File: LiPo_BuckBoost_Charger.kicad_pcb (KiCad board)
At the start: 2 copper layers, 51 parts, among them J1 Type-C_6P, J2 JST PH Connector, J3 Conn_01x01, J4 Conn_01x01, J5 JST PH Connector, J6 Conn_01x01, J7 Conn_01x01, U1 TP4056, U2 DW01A, U3 FS8205A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

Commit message: added schematic and 3d img
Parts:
- added H1: MountingHole, MountingHole:MountingHole_3.2mm_M3_DIN965_Pad, F.Cu at (120.7, 28.3)
- added H2: MountingHole, MountingHole:MountingHole_3.2mm_M3_DIN965_Pad, F.Cu at (74.2, 50.1)
- moved JP1 2.03 mm to (94.8, 52.2)
- moved JP2 2.03 mm to (91.8, 52.2)
- moved JP3 2.03 mm to (88.8, 52.2)
- moved JP4 2.03 mm to (85.8, 52.2)
- moved JP5 2.03 mm to (82.8, 52.2)
- moved JP6 2.03 mm to (79.8, 52.2)
- moved R10 2.03 mm to (82.8, 48.3)
- moved R11 2.03 mm to (79.8, 48.3)
- moved R6 2.03 mm to (94.8, 48.4)
- moved R7 2.03 mm to (91.8, 48.4)
- moved R8 2.03 mm to (88.8, 48.4)
- moved R9 2.03 mm to (85.8, 48.3)
- moved L1 1.86 mm to (101.4, 47.4)
- moved JP7 1.79 mm to (116.2, 31.8)
- moved JP8 1.56 mm to (113.0, 31.8)
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
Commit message: some traces and gnd vias
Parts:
- moved R4 3.25 mm to (79.3, 27.7)
- moved R3 3.03 mm to (82.3, 27.7)
- moved R5 1.65 mm to (89.9, 40.6)
- moved C1 0.38 mm to (88.6, 35.5)
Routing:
- net Net-(JP1-A): track 0.00 -> 42.8 mm, vias 0 -> 2
- net Net-(D1-A): track 0.00 -> 33.2 mm, vias 0 -> 2
- net VBUS: track 0.00 -> 20.7 mm
- net GND: track 0.00 -> 13.3 mm, vias 0 -> 95
- net Net-(U1-STDBY): track 0.00 -> 13.3 mm
- net Net-(D1-K): track 0.00 -> 12.7 mm
- net Net-(U1-CHRG): track 0.00 -> 7.93 mm
- net Net-(J1-CC1): track 0.00 -> 6.54 mm
- net Net-(D2-K): track 0.00 -> 5.15 mm
- net Net-(J1-CC2): track 0.00 -> 4.88 mm
- net Net-(JP5-B): track 0.00 -> 2.20 mm
- net Net-(JP6-B): track 0.00 -> 2.19 mm
- net Net-(JP4-B): track 0.00 -> 2.19 mm
- net Net-(JP1-B): track 0.00 -> 2.18 mm
- net Net-(JP3-B): track 0.00 -> 2.18 mm
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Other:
- copper layers 2 -> 4

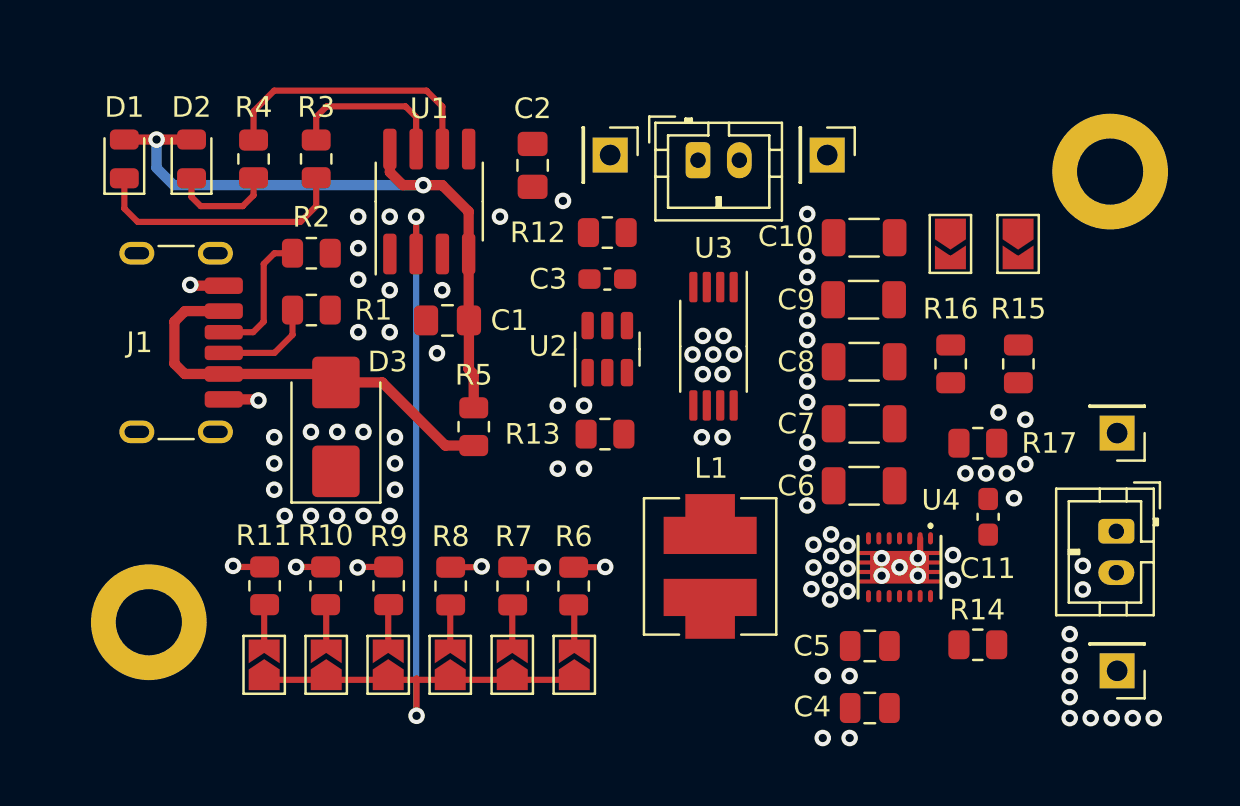
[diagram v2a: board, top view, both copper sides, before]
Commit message: Pcb traces and layout done
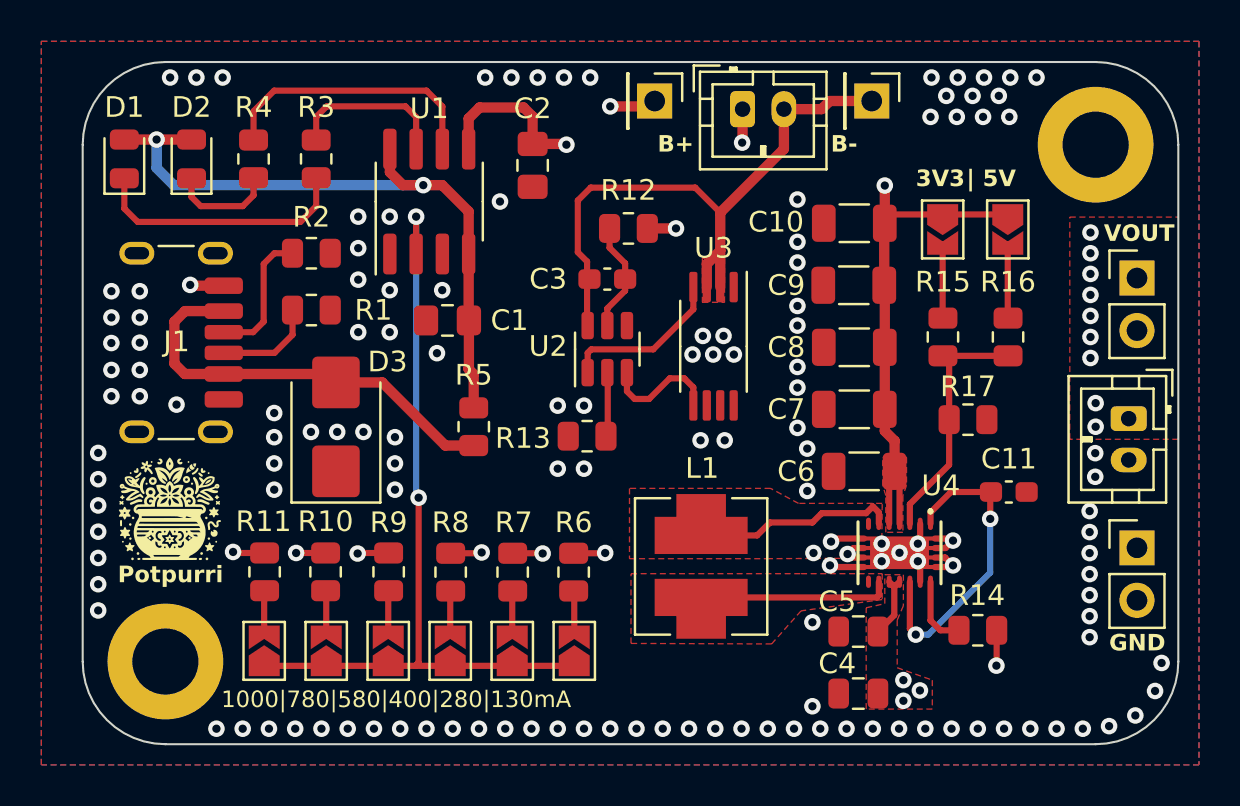
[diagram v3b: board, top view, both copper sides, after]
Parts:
- added G***: LOGO, LOGO, F.Cu at (75.2, 44.7)
- added G***: LOGO, LOGO, B.Cu at (101.7, 50.4)
- J6, J7: value Conn_01x01 -> JST PH Connector; footprint Connector_PinHeader_2.54mm:PinHeader_1x01_P2.54mm_Vertical -> Connector_PinHeader_2.54mm:PinHeader_1x02_P2.54mm_Vertical
- moved J6 7.56 mm to (122.0, 33.5), turned to 0 degrees
- moved J7 6.03 mm to (122.0, 46.5), turned to 0 degrees
- moved J5 5.48 mm to (121.6, 40.2)
- moved R15 3.88 mm to (112.6, 36.3)
- moved JP7 3.72 mm to (112.6, 31.1)
- moved J3 3.39 mm to (98.7, 24.9)
- moved J4 3.39 mm to (109.2, 24.9)
- moved J2 3.28 mm to (102.9, 25.3)
- moved R16 3.07 mm to (115.8, 36.3)
- moved JP8 2.86 mm to (115.8, 31.1)
- moved H2 2.06 mm to (75.0, 52.0)
- moved C11 1.56 mm to (115.8, 43.8), turned to 0 degrees
- moved H1 1.48 mm to (120.0, 27.0)
- moved R17 1.23 mm to (113.8, 40.3)
- moved R12 1.04 mm to (97.4, 31.1), turned to 0 degrees
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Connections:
- U4 pad 13: Net-(U4-EN) -> GND
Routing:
- net -BATT: track 0.00 -> 30.3 mm
- net +5V: track 0.00 -> 27.2 mm, vias 0 -> 11
- net +BATT: track 0.00 -> 16.5 mm, vias 0 -> 7
- net Net-(U4-EN): track 0.00 -> 15.3 mm, vias 0 -> 2
- net GND: track 13.3 -> 25.8 mm, vias 95 -> 146
- net Net-(U4-FB): track 0.00 -> 12.2 mm
- net Net-(L1-Pad2): track 0.00 -> 9.85 mm
- net Net-(L1-Pad1): track 0.00 -> 9.30 mm
- net Net-(U2-OD): track 0.00 -> 8.01 mm
- net Net-(U2-OC): track 0.00 -> 5.74 mm
- net Net-(U2-VCC): track 0.00 -> 5.44 mm
- net Net-(JP1-A): track 42.8 -> 38.7 mm
- net Net-(JP8-B): track 0.00 -> 3.57 mm
- net Net-(JP7-B): track 0.00 -> 3.57 mm
- net Net-(U4-PG): track 0.00 -> 3.45 mm
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- added copper zone on F.Cu, net +5V
- added copper zone on In2.Cu, net +5V
- added copper zone on F.Cu, net +BATT
- added copper zone on In2.Cu, net +BATT
- added copper zone on F.Cu, net -BATT
- added copper zone on B.Cu, net GND
- added copper zone on F.Cu, net GND
- added copper zone on In1.Cu, net GND
- added copper zone on F.Cu, net Net-(L1-Pad1)
- added copper zone on F.Cu, net Net-(L1-Pad2)
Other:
- board outline added: 53 x 33 mm
- board text added: "1000|780|580|400|280|130mA"
- board text added: "3V3"
- board text added: "B+"
- board text added: "B-"
- board text added: "GND"
- board text added: "Potpurri"
- board text added: "Potpurri TP4056 LiPo Charger with TPS63020 Buck-Boost Converter Version 1.0"
- board text added: "VOUT"
- board text added: "| 5V"

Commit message: added fillet tracks and tear drops to pcb
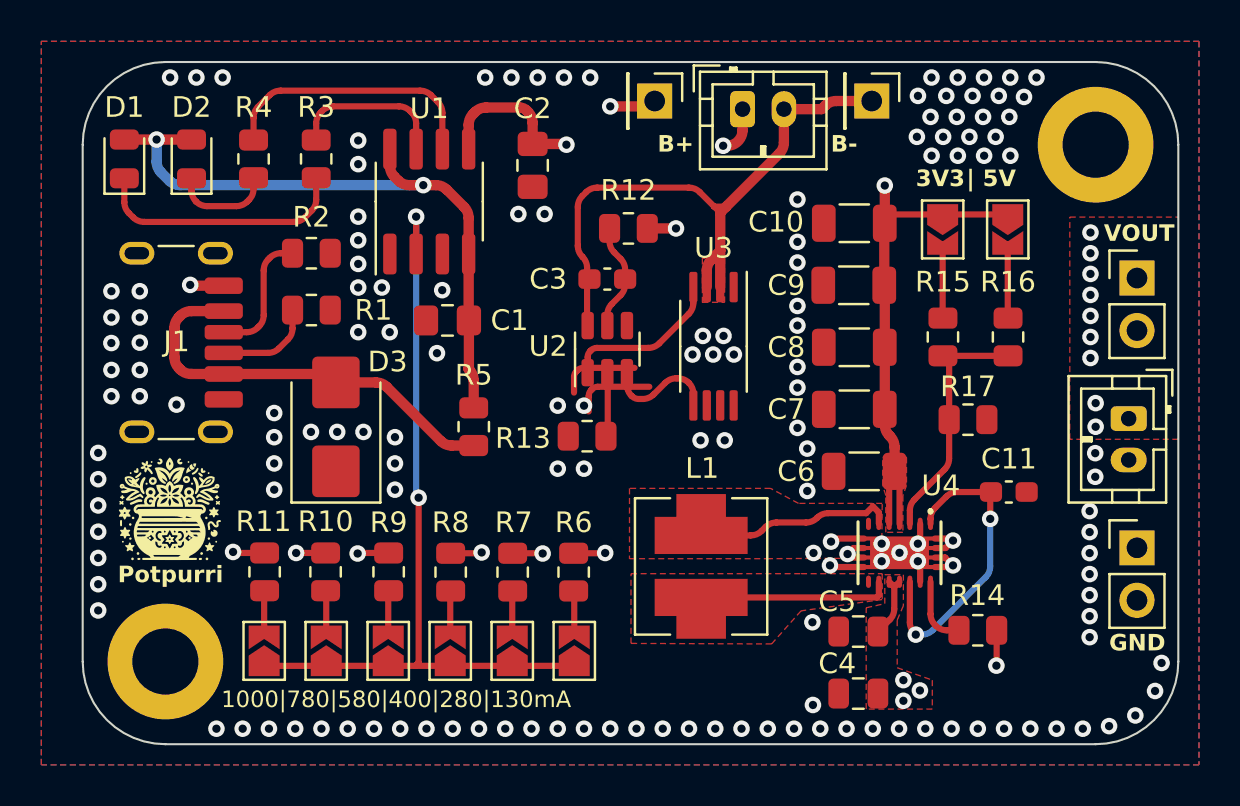
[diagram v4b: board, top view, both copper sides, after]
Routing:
- net Net-(U2-OD): track 8.01 -> 15.7 mm
- net +BATT: track 16.5 -> 17.0 mm
- net GND: vias 146 -> 159

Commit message: Version 1.1 - added 2512 footprint for input resistor to TP4056
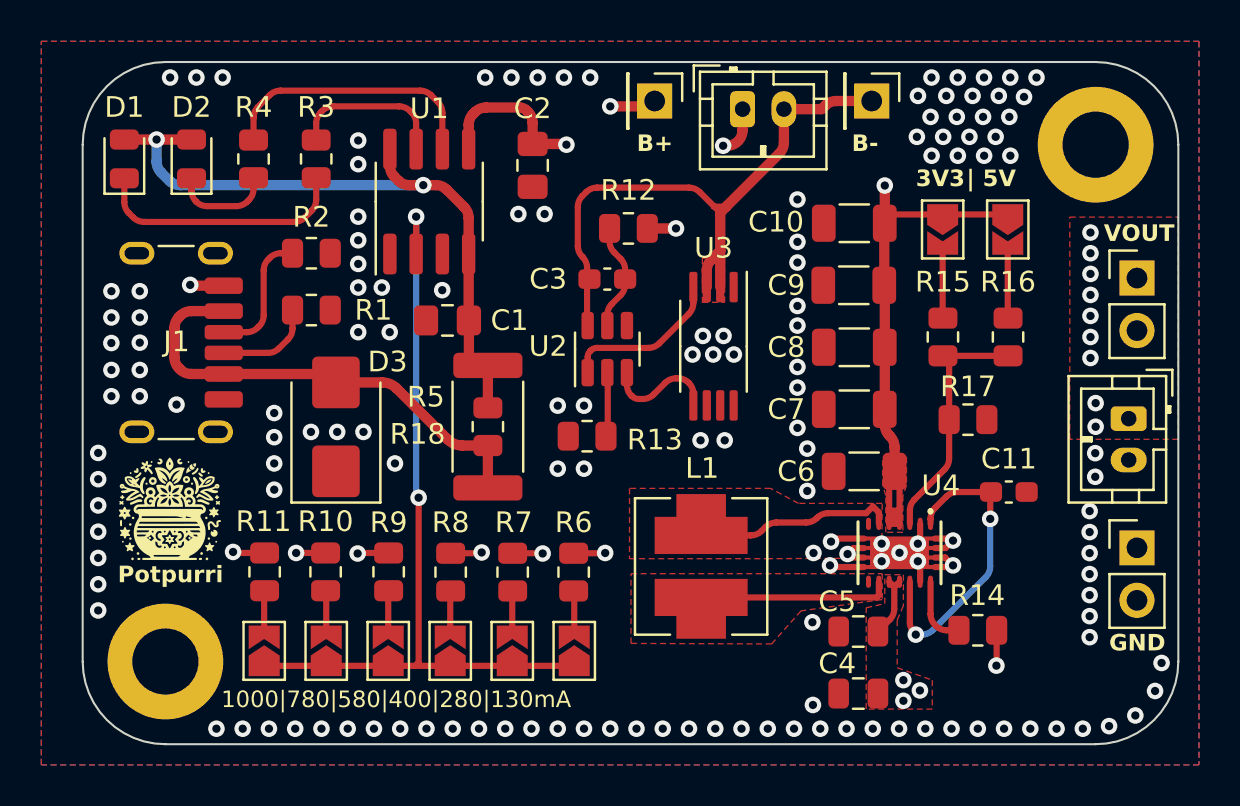
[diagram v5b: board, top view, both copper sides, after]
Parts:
- added R18: 2512 package, Resistor_SMD:R_2512_6332Metric, F.Cu at (90.6, 40.6)
- moved R5 0.68 mm to (90.6, 40.6)
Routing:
- net Net-(U2-OD): track 15.7 -> 7.88 mm
- net VBUS: track 20.5 -> 23.2 mm
- net +5V: track 27.1 -> 29.2 mm
- net Net-(D1-A): track 32.9 -> 33.8 mm
- net GND: vias 159 -> 156
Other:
- board text added: "Potpurri TP4056 LiPo Charger with TPS63020 Buck-Boost Converter Version 1.1"
- board text removed: "Potpurri TP4056 LiPo Charger with TPS63020 Buck-Boost Converter Version 1.0"

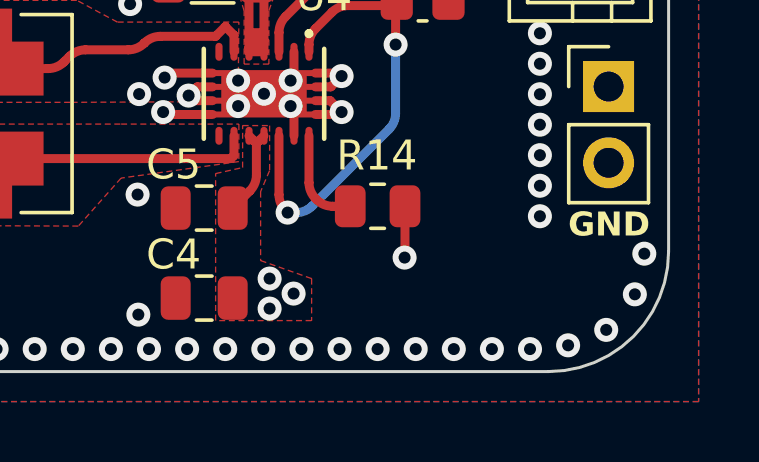
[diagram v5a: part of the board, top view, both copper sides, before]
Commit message: Added jlc serial number silk screen
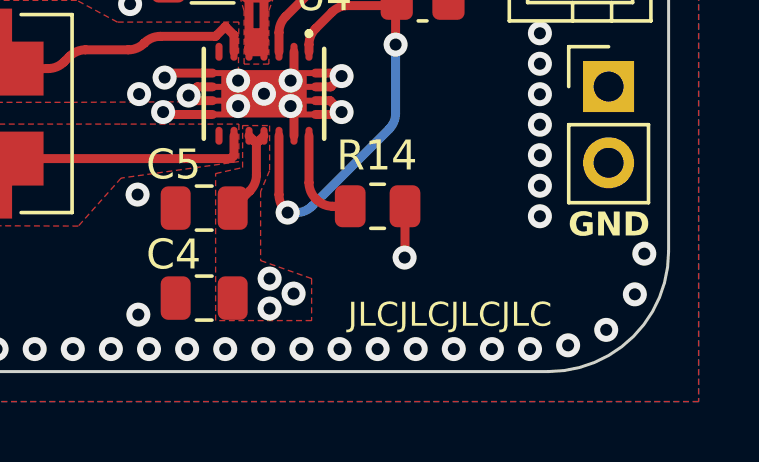
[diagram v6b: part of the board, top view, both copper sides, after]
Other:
- board text added: "JLCJLCJLCJLC"
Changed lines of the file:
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@@
     (effects (font (size 0.8 0.8) (thickness 0.15) bold) (justify left bottom))
+  )
+  (gr_text "JLCJLCJLCJLC" (at 116.713 54.102) (layer "F.SilkS")
+    (effects (font (size 0.8 0.8) (thickness 0.1)))
   )
   (gr_text "B-" (at 108.2 27.4) (layer "F.SilkS")

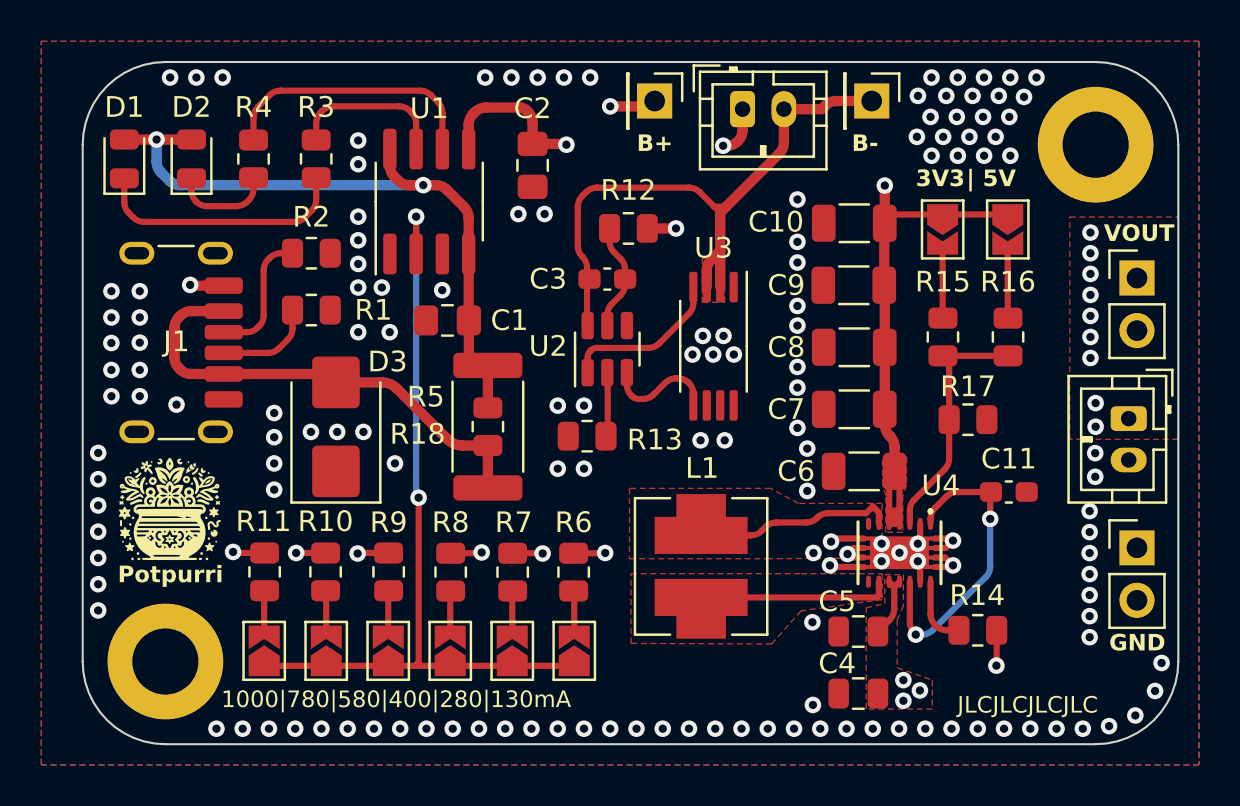
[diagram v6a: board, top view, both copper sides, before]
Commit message: v1.2, fixed filled zones for inductor
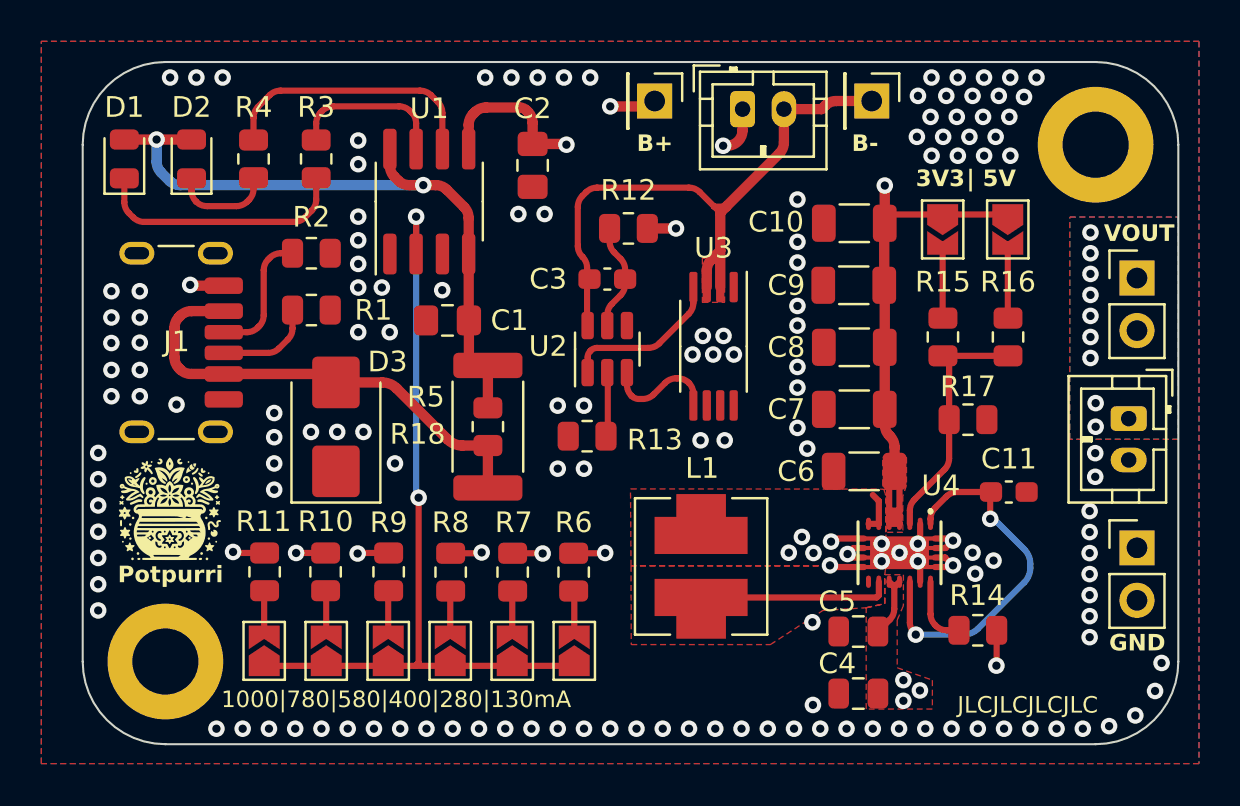
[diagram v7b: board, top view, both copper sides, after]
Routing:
- net Net-(L1-Pad2): track 9.70 -> 2.02 mm
- net Net-(U4-EN): track 15.1 -> 18.0 mm
- net GND: vias 156 -> 160
- added copper zone on B.Cu, net +5V
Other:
- board text added: "Potpurri TP4056 LiPo Charger with TPS63020 Buck-Boost Converter Version 1.2"
- board text removed: "Potpurri TP4056 LiPo Charger with TPS63020 Buck-Boost Converter Version 1.1"
